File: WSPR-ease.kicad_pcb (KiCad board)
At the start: 4 copper layers, 99.2 x 74.8 mm, 110 parts, among them J1 GNSS Ant, J2 Tx Ant, J3 USB_C_16P_Stacked, Q1 MMBF170, Q10 MMBF170, Q11 MMBF170, Q12 MMBF170, Q13 MMBF170, Q2 MMBF170, Q3 MMBF170, Q4 MMBF170, Q5 MMBF170, Q6 MMBF170, Q7 MMBF170, Q8 MMBF170, Q9 MMBF170, T1 BN-43-202_DualPri_CTSec, U1 ESP32-S3-WROOM-1, U2 NCP1117-3.3_SOT223, U3 ATGM336H-5N31, U4 ICE40UP5K-SG48ITR, U5 TLV70012, U6 CD74ACT541M96G4

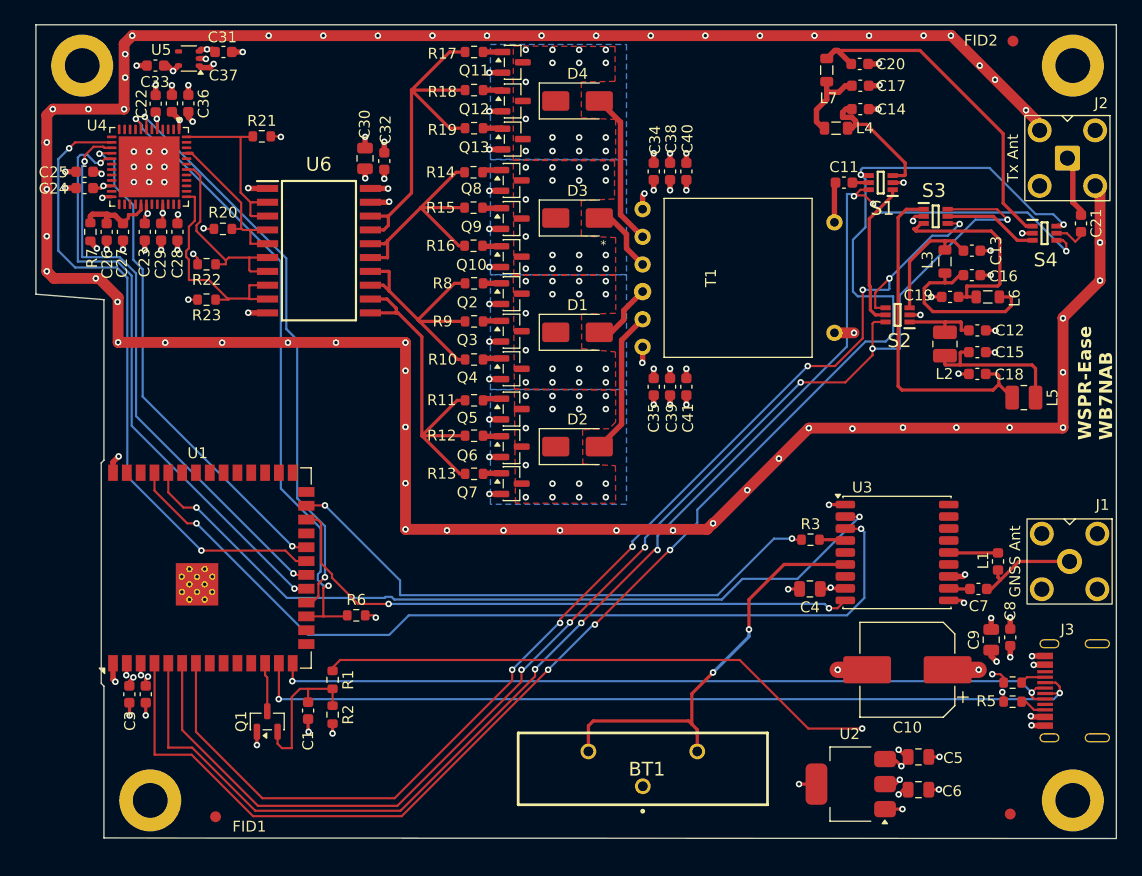
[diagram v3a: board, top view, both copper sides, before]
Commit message: Cleanup. Better USB diff pair with 0ohm and TVS as recommended. Return to rectangular outline and even smaller. Mounting holes are consistently placed relative to board corners.
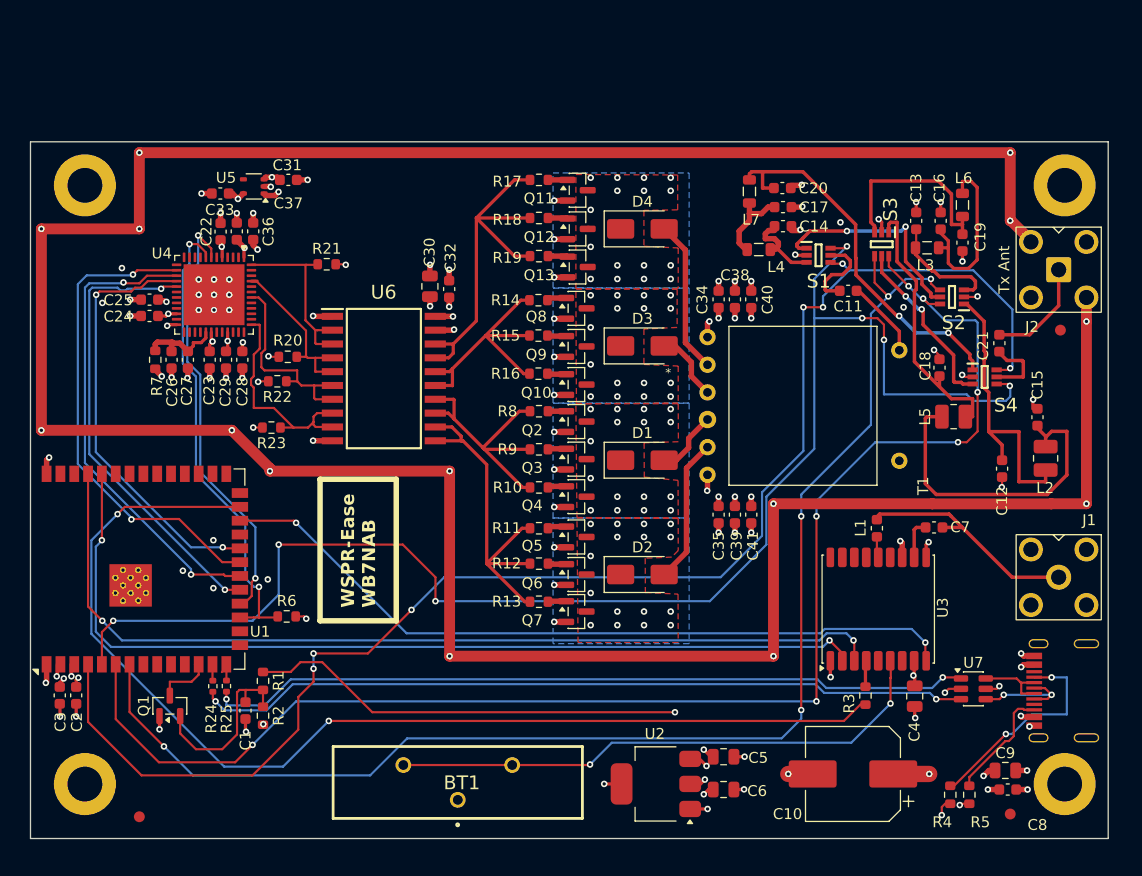
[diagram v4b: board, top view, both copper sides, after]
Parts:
- added R24: 0, Resistor_SMD:R_0402_1005Metric, F.Cu at (66.3, 119.4)
- added R25: 0, Resistor_SMD:R_0402_1005Metric, F.Cu at (67.6, 119.4)
- added U7: SRV05-4, Package_TO_SOT_SMD:SOT-23-6, F.Cu at (136.2, 119.7)
- C1, C11, C21: value 100nF -> 100nF X7R
- C10: value 100uF -> 100uF X7R 25V
- C12, C16, C18: value 470pF -> 470pF NP0
- C13, C17, C19: value 220pF -> 220pF NP0
- C14, C20: value 100pF -> 100pF NP0
- C15: value 1nF -> 1nF NP0
- C2, C22, C24, C26, C28, C32, C36: value 0.1uF -> 100nF X7R
- C23, C25, C27, C29, C30, C37, C4, C5, C6: value 10uF -> 10uF X7R
- C3: value 22uF -> 10uF X7R
- C31, C33: value 1uF -> 1uF X7R
- C34, C35: value 10uF X7R -> 10uF X7R 25V
- C38, C39: value 0.1uF X7R -> 100nF X7R 50V
- C8: value 100nF -> 100nF X7R 50V
- C9: value 10uF -> 10uF X7R 50V
- U1: value ESP32-S3-WROOM-1 -> ESP32-S3-WROOM-1-N8R8
- moved FID2 26.9 mm to (144.2, 86.7)
- moved U2 17.9 mm to (107.0, 128.4)
- moved C5 17.9 mm to (113.3, 125.9)
- moved C6 17.9 mm to (113.3, 128.9)
- moved BT1 17.0 mm to (88.8, 128.2)
- moved R3 15.2 mm to (126.3, 120.3), turned to 90 degrees
- moved S4 14.3 mm to (137.2, 91.0)
- moved L2 14.0 mm to (142.8, 98.5), turned to 90 degrees
- moved C8 14.0 mm to (139.4, 128.9), turned to 0 degrees
- moved C4 13.8 mm to (130.8, 120.3), turned to -90 degrees
- moved C20 13.4 mm to (118.7, 73.7)
- moved C21 13.3 mm to (138.6, 87.9)
- moved C17 13.2 mm to (118.7, 75.4)
- moved L7 13.2 mm to (115.6, 74.0)
- moved L4 13.2 mm to (116.5, 79.3)
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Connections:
- J3 pad A6: /D+ -> Net-(U7-IO3)
- J3 pad A7: /D- -> Net-(U7-IO4)
- J3 pad B6: /D+ -> Net-(U7-IO3)
- J3 pad B7: /D- -> Net-(U7-IO4)
- U1 pad 13: /D- -> Net-(U1-USB_D-)
- U1 pad 14: /D+ -> Net-(U1-USB_D+)
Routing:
- net Net-(U1-IO48): track 51.9 -> 101.7 mm
- net Net-(S2-J2): track 7.15 -> 26.9 mm
- net Net-(J3-CC1): track 2.36 -> 19.8 mm, vias 0 -> 2
- net Net-(C15-Pad1): track 13.9 -> 30.1 mm
- net /fpgaNRESET: track 59.9 -> 43.8 mm
- net /fpgaMISO: track 59.2 -> 44.6 mm
- net /gnssNRESET: track 55.5 -> 69.9 mm
- net /fpgaMOSI: track 54.8 -> 42.1 mm
- net /lo2ON: track 110.5 -> 123.0 mm, vias 7 -> 5
- net /fpgaDONE: track 53.7 -> 41.2 mm
- net Net-(U3-V_BCKP): track 38.7 -> 50.7 mm
- net Net-(J1-In): track 9.65 -> 21.3 mm
- net VBUS: track 73.9 -> 62.4 mm
- net /gnssTx: track 73.9 -> 85.3 mm
- net /lo1ON: track 121.0 -> 132.2 mm, vias 6 -> 7
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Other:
- board size 99.2 x 74.8 mm -> 99 x 64 mm

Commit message: Add stitching vias to ground ring around RF zone
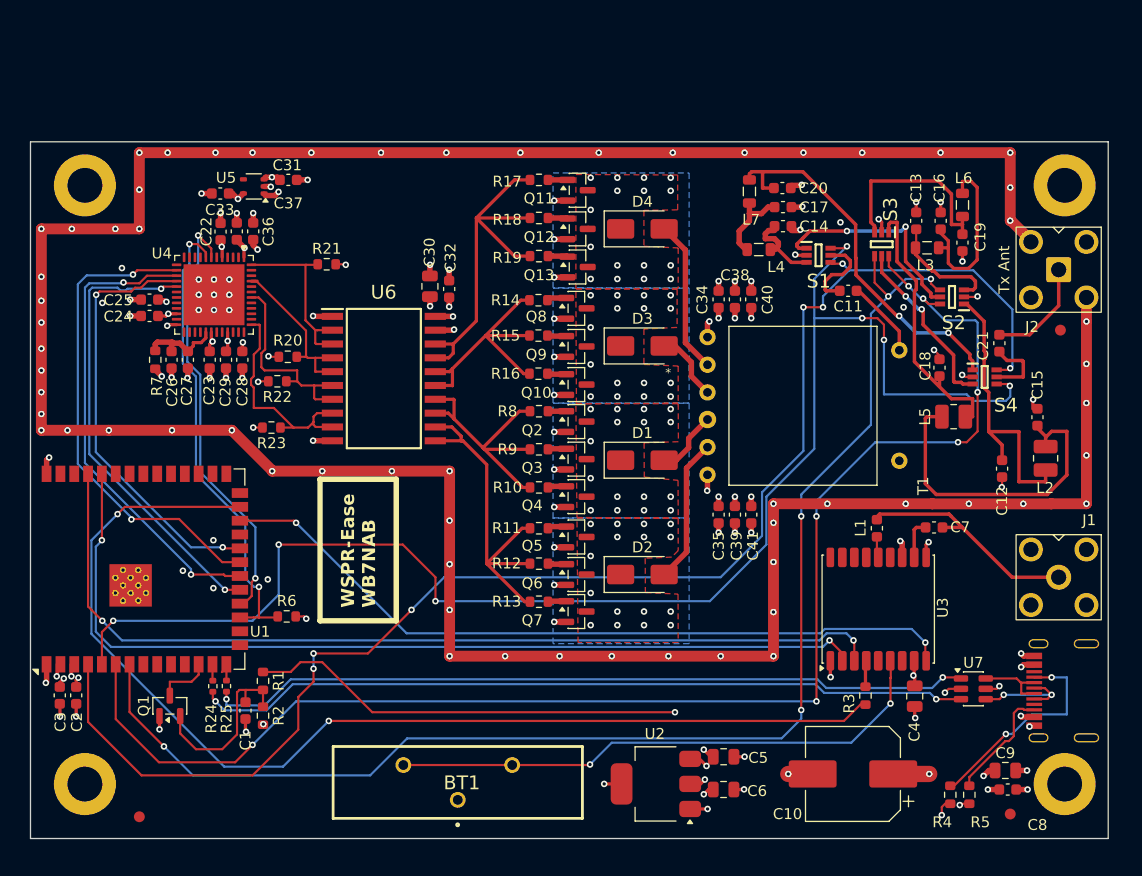
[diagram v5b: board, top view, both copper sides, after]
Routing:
- net GND: track 353.9 -> 353.8 mm, vias 106 -> 153

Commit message: Switch to SSOP package for 74ACT541. Tweak a bunch of layout for DFM and maybe some improved SI.
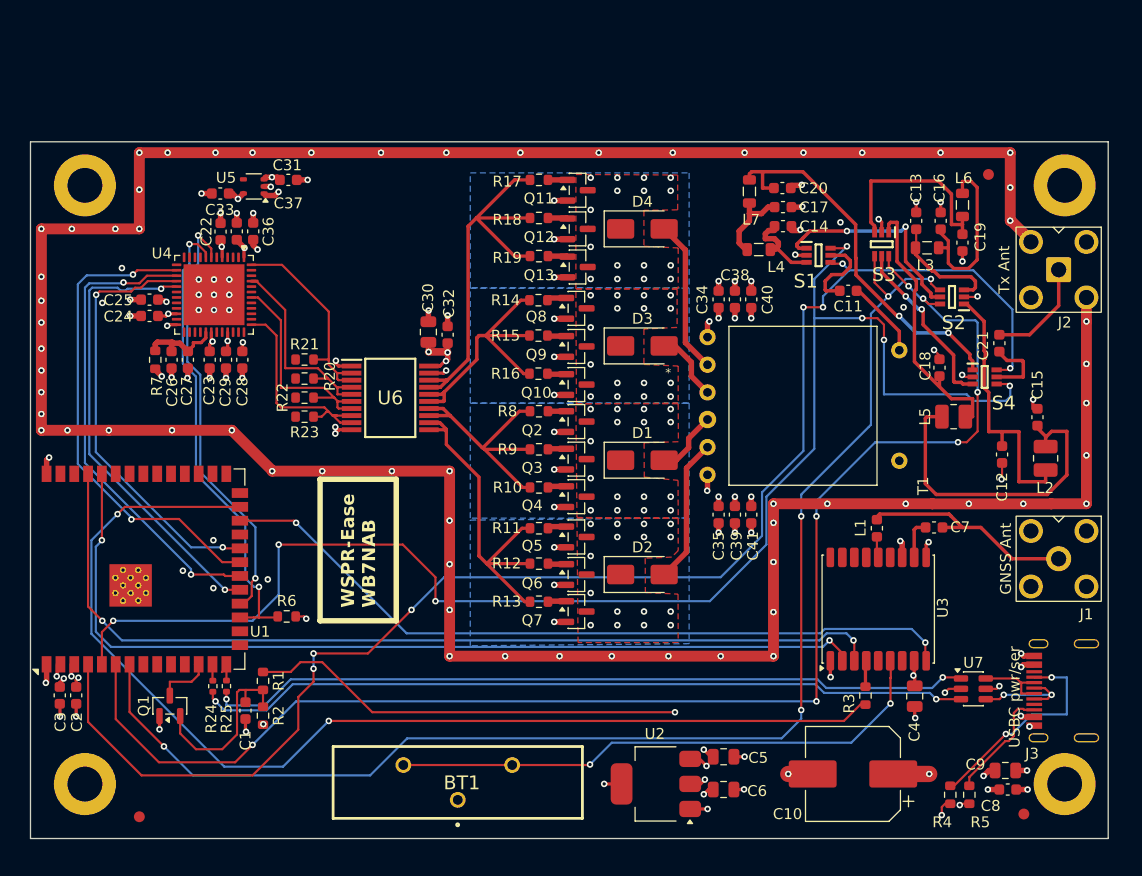
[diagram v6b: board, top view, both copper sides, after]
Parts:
- J3: value USB_C_16P_Stacked -> USBC pwr/ser
- U6: value CD74ACT541M96G4 -> CD74ACT541SM96; footprint Library:SOIC127P1030X265-20N -> Library:SOP65P780X200-20N
- moved FID2 15.8 mm to (137.6, 72.4)
- moved R21 8.98 mm to (74.8, 89.4), turned to 180 degrees
- moved C30 4.20 mm to (86.2, 86.9)
- moved C32 4.20 mm to (87.9, 87.1)
- moved R23 3.20 mm to (74.8, 94.7)
- moved R22 2.92 mm to (74.8, 92.9)
- moved R20 2.52 mm to (74.8, 91.2)
- moved U6 1.87 mm to (82.7, 92.9)
- moved J1 1.70 mm to (144.1, 107.7)
- moved C12 1.30 mm to (138.8, 98.1)
- moved FID3 1.25 mm to (140.8, 131.2)
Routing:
- net /Transmitter/pull1: track 16.0 -> 20.2 mm
- net GND: track 353.8 -> 350.9 mm, vias 153 -> 150
- net /Transmitter/pull2G: track 34.5 -> 37.3 mm
- net +3.3V: track 25.8 -> 28.6 mm
- net /Transmitter/pull2: track 16.9 -> 19.5 mm
- net Net-(S2-J2): track 26.9 -> 25.2 mm
- net /Transmitter/pull1G: track 24.0 -> 25.7 mm
- net /Transmitter/push1: track 19.2 -> 20.6 mm
- net /Transmitter/push1G: track 24.9 -> 24.1 mm
- net Net-(J1-In): track 21.3 -> 20.6 mm
- net /Transmitter/push2: track 20.9 -> 20.3 mm

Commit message: Fix up 3d in footprints in lib so they stay put when I update PCB from schematic. Fix text labels for same issue.
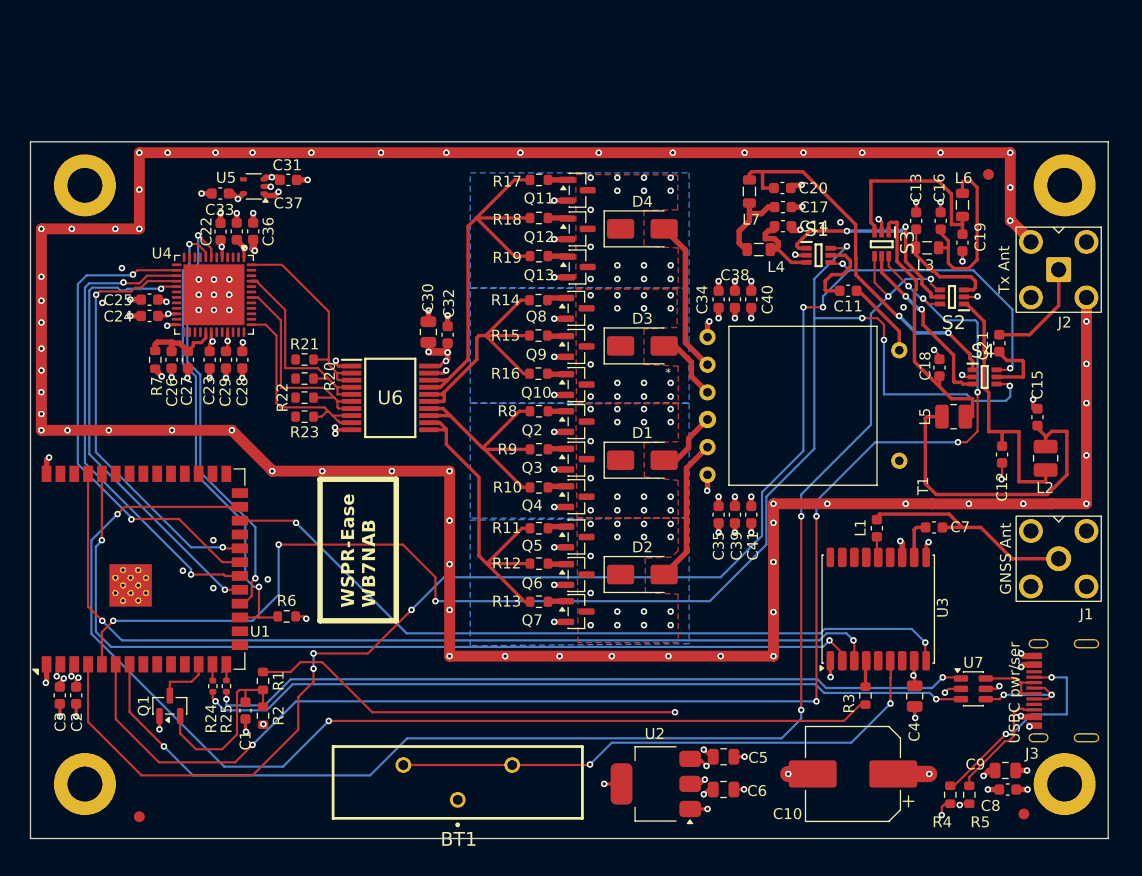
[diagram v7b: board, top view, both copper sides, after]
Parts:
- C10: value 100uF X7R 25V -> 100uF 35V
- C23, C25, C27, C29, C3, C37: value 10uF X7R -> 10uF X5R
- C30, C4, C5, C6: value 10uF X7R -> 10uF 16V X5R
- C31, C33: value 1uF X7R -> 1uF X7R 25V
- C9: value 10uF X7R 50V -> 10uF 16V X5R
- J3: value USBC pwr/ser -> USB_C_16P_Stacked
